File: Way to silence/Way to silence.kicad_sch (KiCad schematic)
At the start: 3 parts, among them U1 ESP32-WROOM-32-N16, U2 SM5308, U4 MAX98357AETE+T

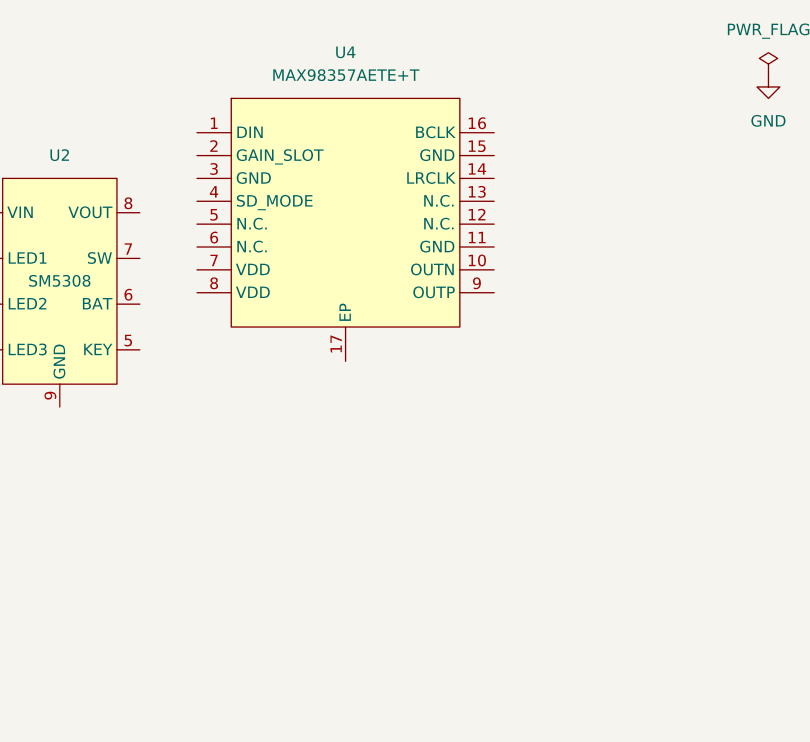
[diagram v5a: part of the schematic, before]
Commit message: [ADD] I2S AMP Sheet
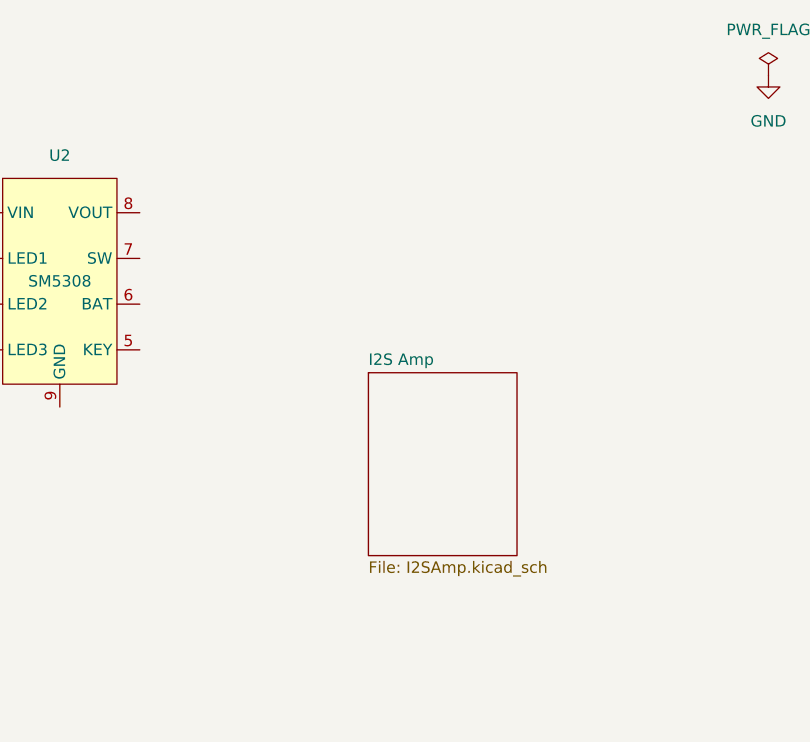
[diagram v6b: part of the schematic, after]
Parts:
- removed U4: MAX98357AETE+T, Way to silence:MAX98357, symbol Way to silence:MAX98357
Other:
- added sheet I2S Amp (I2SAmp.kicad_sch)
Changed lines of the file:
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@@
-    )
-  )
-  (symbol (lib_id "Way to silence:MAX98357") (at 118.11 40.64 0) (unit 1)
-    (in_bom yes) (on_board yes) (dnp no) (fields_autoplaced)
-    (property "Reference" "U4" (at 118.11 22.86 0)
-      (effects (font (size 1.27 1.27)))
-    )
-    (property "Value" "MAX98357AETE+T" (at 118.11 25.4 0)
-      (effects (font (size 1.27 1.27)))
-    )
-    (property "Footprint" "Way to silence:MAX98357" (at 118.11 40.64 0)
-      (effects (font (size 1.27 1.27)) hide)
-    )
-    (property "Datasheet" "" (at 118.11 40.64 0)
-      (effects (font (size 1.27 1.27)) hide)
-    )
-    (pin "1")
-    (pin "10")
-    (pin "11")
-    (pin "12")
-    (pin "13")
-    (pin "14")
-    (pin "15")
-    (pin "16")
-    (pin "17")
-    (pin "2")
-    (pin "3")
-    (pin "4")
-    (pin "5")
-    (pin "6")
-    (pin "7")
-    (pin "8")
-    (pin "9")
-    (instances
-      (project "Way to silence"
-        (path "/9822a1be-a034-44c3-8530-56368958b215"
-          (reference "U4") (unit 1)
-        )
-      )
     )
   )
@@
       )
     )
+  )
+  (sheet (at 120.65 58.42) (size 16.51 20.32) (fields_autoplaced)
+    (stroke (width 0.1524) (type solid))
+    (fill (color 0 0 0 0.0000))
+    (property "Sheetname" "I2S Amp" (at 120.65 57.7084 0)
+      (effects (font (size 1.27 1.27)) (justify left bottom))
+    )
+    (property "Sheetfile" "I2SAmp.kicad_sch" (at 120.65 79.3246 0)
+      (effects (font (size 1.27 1.27)) (justify left top))
+    )
+    (instances
+      (project "Way to silence"
+        (path "/9822a1be-a034-44c3-8530-56368958b215" (page "4"))
+      )
+    )

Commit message: [DRC] I2S Amp seems Sheet ok
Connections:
- no-connect marks 9 -> 14
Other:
- sheet I2S Amp ports: added BCLK, DIN, GAIN, LRCLK, SD; removed none
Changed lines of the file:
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@@
 (kicad_sch (version 20230121) (generator eeschema)
   (paper "A4")
+  (no_connect (at 120.65 71.12))
+  (no_connect (at 120.65 66.04))
+  (no_connect (at 120.65 68.58))
   (no_connect (at 176.53 95.25))
   (no_connect (at 199.39 60.96))
+  (no_connect (at 120.65 60.96))
+  (no_connect (at 120.65 63.5))
   (no_connect (at 199.39 63.5))
   (no_connect (at 176.53 92.71))
@@
     )
   )
-  (sheet (at 120.65 58.42) (size 16.51 20.32) (fields_autoplaced)
+  (sheet (at 120.65 58.42) (size 16.51 15.24) (fields_autoplaced)
     (stroke (width 0.1524) (type solid))
     (fill (color 0 0 0 0.0000))
@@
       (effects (font (size 1.27 1.27)) (justify left bottom))
     )
-    (property "Sheetfile" "I2SAmp.kicad_sch" (at 120.65 79.3246 0)
+    (property "Sheetfile" "I2SAmp.kicad_sch" (at 120.65 74.2446 0)
       (effects (font (size 1.27 1.27)) (justify left top))
+    )
+    (pin "BCLK" bidirectional (at 120.65 60.96 180)
+      (effects (font (size 1.27 1.27)) (justify left))
+    )
+    (pin "LRCLK" bidirectional (at 120.65 63.5 180)
+      (effects (font (size 1.27 1.27)) (justify left))
+    )
+    (pin "GAIN" bidirectional (at 120.65 66.04 180)
+      (effects (font (size 1.27 1.27)) (justify left))
+    )
+    (pin "DIN" bidirectional (at 120.65 68.58 180)
+      (effects (font (size 1.27 1.27)) (justify left))
+    )
+    (pin "SD" bidirectional (at 120.65 71.12 180)
+      (effects (font (size 1.27 1.27)) (justify left))
     )
     (instances
@@
     )
   )
-  (sheet (at 176.53 85.09) (size 15.24 11.43) (fields_autoplaced)
+  (sheet (at 176.53 85.09) (size 15.24 12.7) (fields_autoplaced)
     (stroke (width 0.1524) (type solid))
     (fill (color 0 0 0 0.0000))
@@
       (effects (font (size 1.27 1.27)) (justify left bottom))
     )
-    (property "Sheetfile" "USB to Uart.kicad_sch" (at 176.53 97.1046 0)
+    (property "Sheetfile" "USB to Uart.kicad_sch" (at 176.53 98.3746 0)
       (effects (font (size 1.27 1.27)) (justify left top))
     )

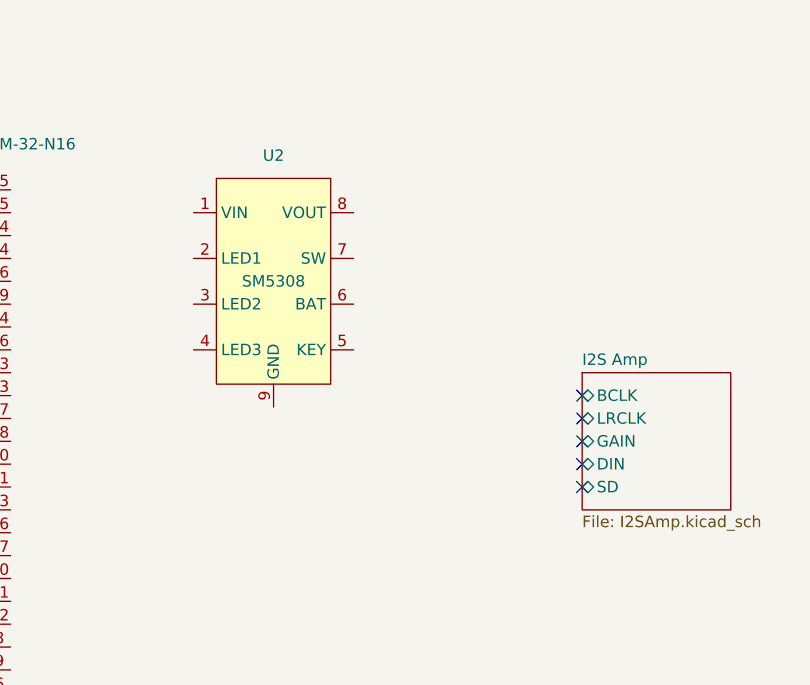
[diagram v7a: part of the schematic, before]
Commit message: [ADD] BMS Sheet
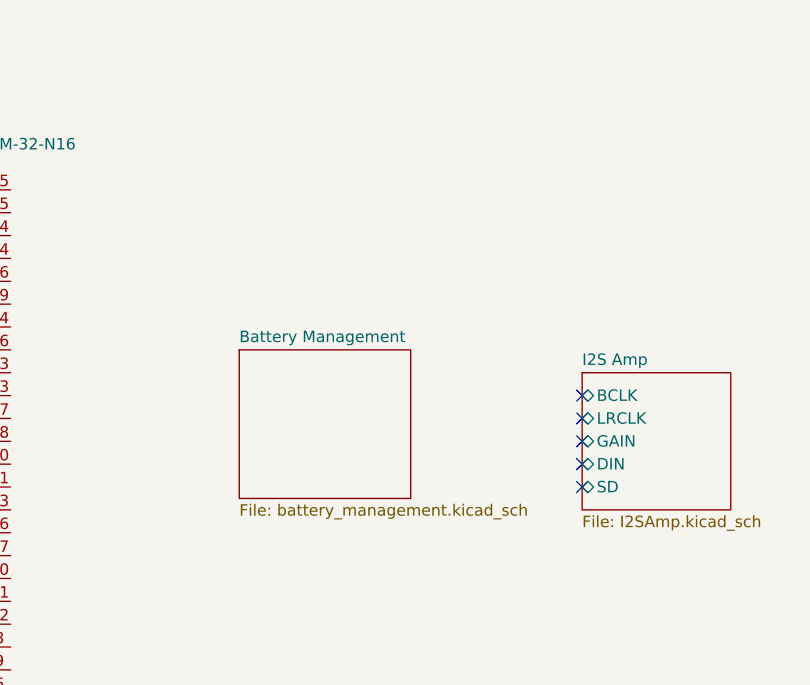
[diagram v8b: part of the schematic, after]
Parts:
- removed U2: SM5308, Way to silence:SM5308, symbol Way to silence:SM5308
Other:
- added sheet Battery Management (battery_management.kicad_sch)
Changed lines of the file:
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@@
-    )
-  )
-  (symbol (lib_id "Way to silence:SM5308") (at 86.36 48.26 0) (unit 1)
-    (in_bom yes) (on_board yes) (dnp no) (fields_autoplaced)
-    (property "Reference" "U2" (at 86.36 34.29 0)
-      (effects (font (size 1.27 1.27)))
-    )
-    (property "Value" "SM5308" (at 86.36 48.26 0)
-      (effects (font (size 1.27 1.27)))
-    )
-    (property "Footprint" "Way to silence:SM5308" (at 86.36 48.26 0)
-      (effects (font (size 1.27 1.27)) hide)
-    )
-    (property "Datasheet" "https://datasheet.lcsc.com/lcsc/2301051530_HICHON-SM5308_C5345582.pdf" (at 86.36 48.26 0)
-      (effects (font (size 1.27 1.27)) hide)
-    )
-    (property "LCSC" "C5345582" (at 86.36 48.26 0)
-      (effects (font (size 1.27 1.27)) hide)
-    )
-    (pin "1")
-    (pin "2")
-    (pin "3")
-    (pin "4")
-    (pin "5")
-    (pin "6")
-    (pin "7")
-    (pin "8")
-    (pin "9")
-    (instances
-      (project "Way to silence"
-        (path "/9822a1be-a034-44c3-8530-56368958b215"
-          (reference "U2") (unit 1)
-        )
-      )
     )
   )
@@
       )
     )
+  )
+  (sheet (at 82.55 55.88) (size 19.05 16.51) (fields_autoplaced)
+    (stroke (width 0.1524) (type solid))
+    (fill (color 0 0 0 0.0000))
+    (property "Sheetname" "Battery Management" (at 82.55 55.1684 0)
+      (effects (font (size 1.27 1.27)) (justify left bottom))
+    )
+    (property "Sheetfile" "battery_management.kicad_sch" (at 82.55 72.9746 0)
+      (effects (font (size 1.27 1.27)) (justify left top))
+    )
+    (instances
+      (project "Way to silence"
+        (path "/9822a1be-a034-44c3-8530-56368958b215" (page "5"))
+      )
+    )
